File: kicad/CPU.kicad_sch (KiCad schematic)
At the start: 32 parts, among them J1 Conn_01x01_Pin, J2 Conn_01x06_Pin, J3 Conn_01x01_Pin, J4 Conn_01x01_Pin, J5 Conn_01x01_Pin, U10 GAL22V10, U11 AS6C4008-55PCN, U12 AS6C4008-55PCN, U12 GAL22V10, U13 74LS245, U14 74LS245, U3 74LS244, U5 SST39SF040, U6 SST39SF040, U7 68010P10, U8 74LS244, U9 74LS244

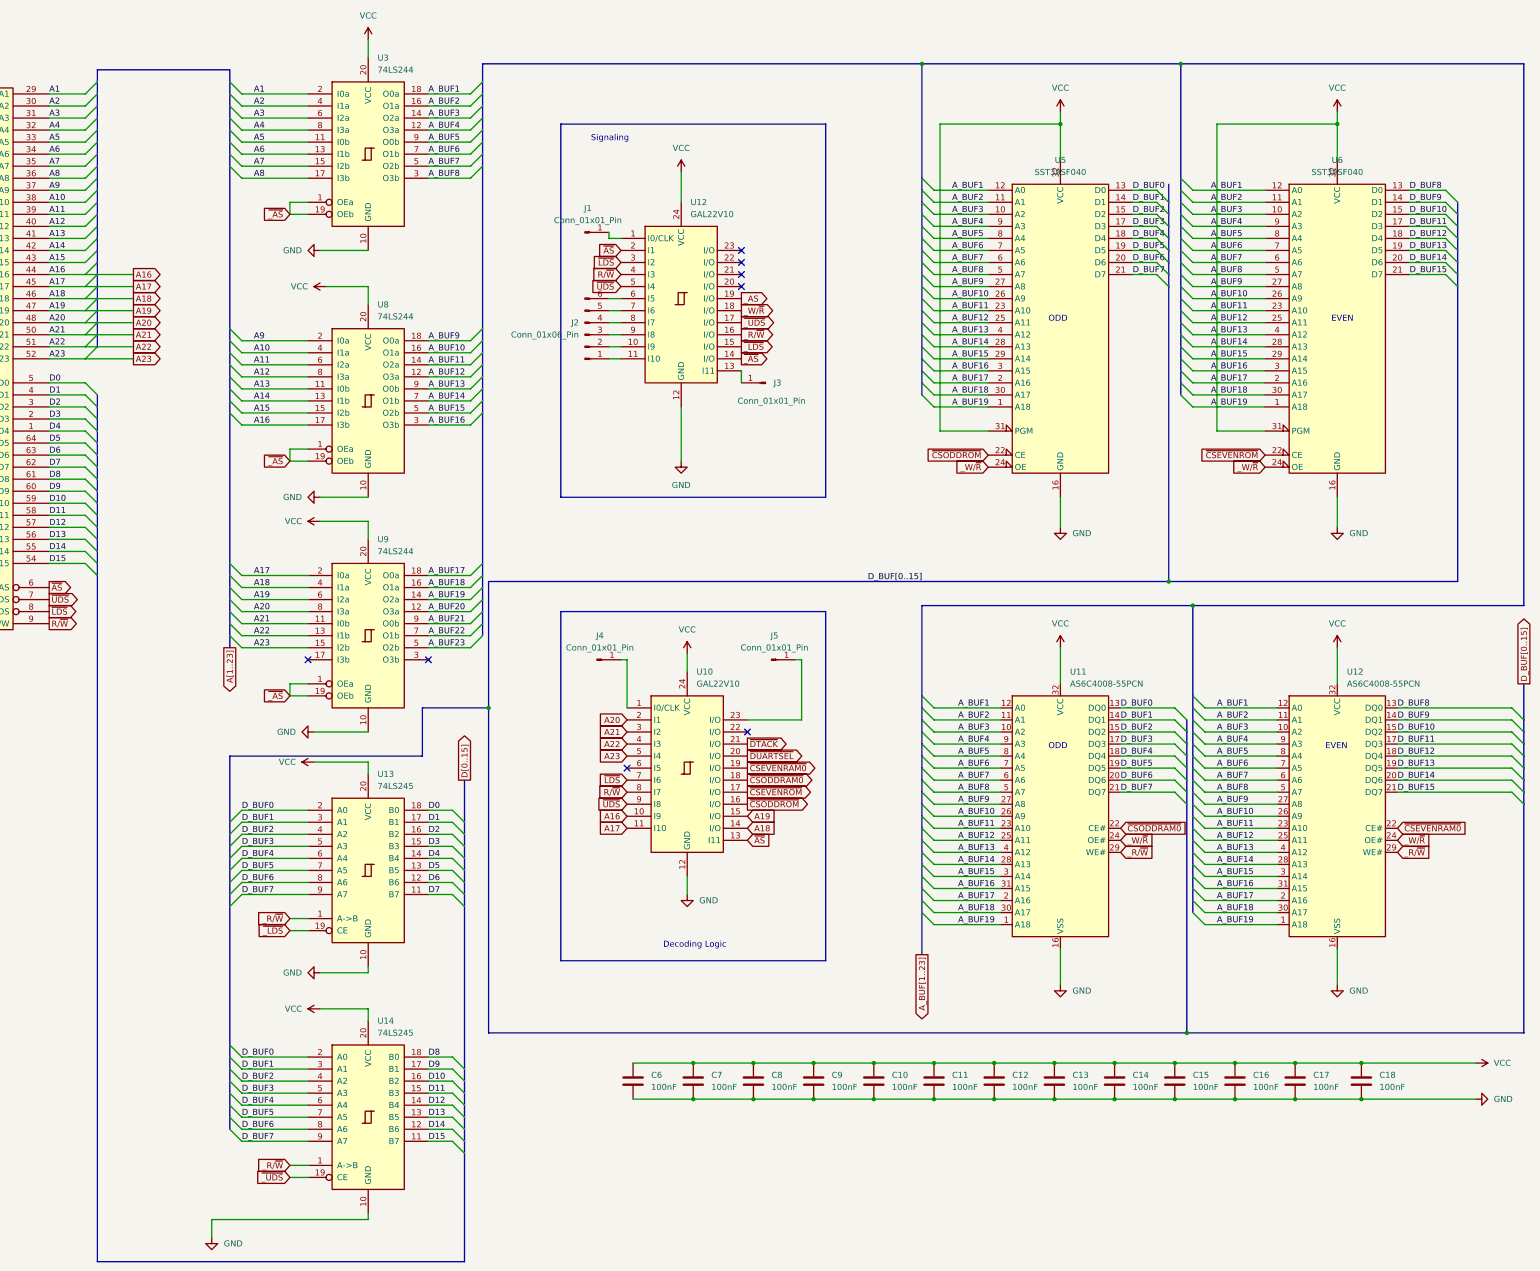
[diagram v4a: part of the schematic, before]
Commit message: PCB to ATX size
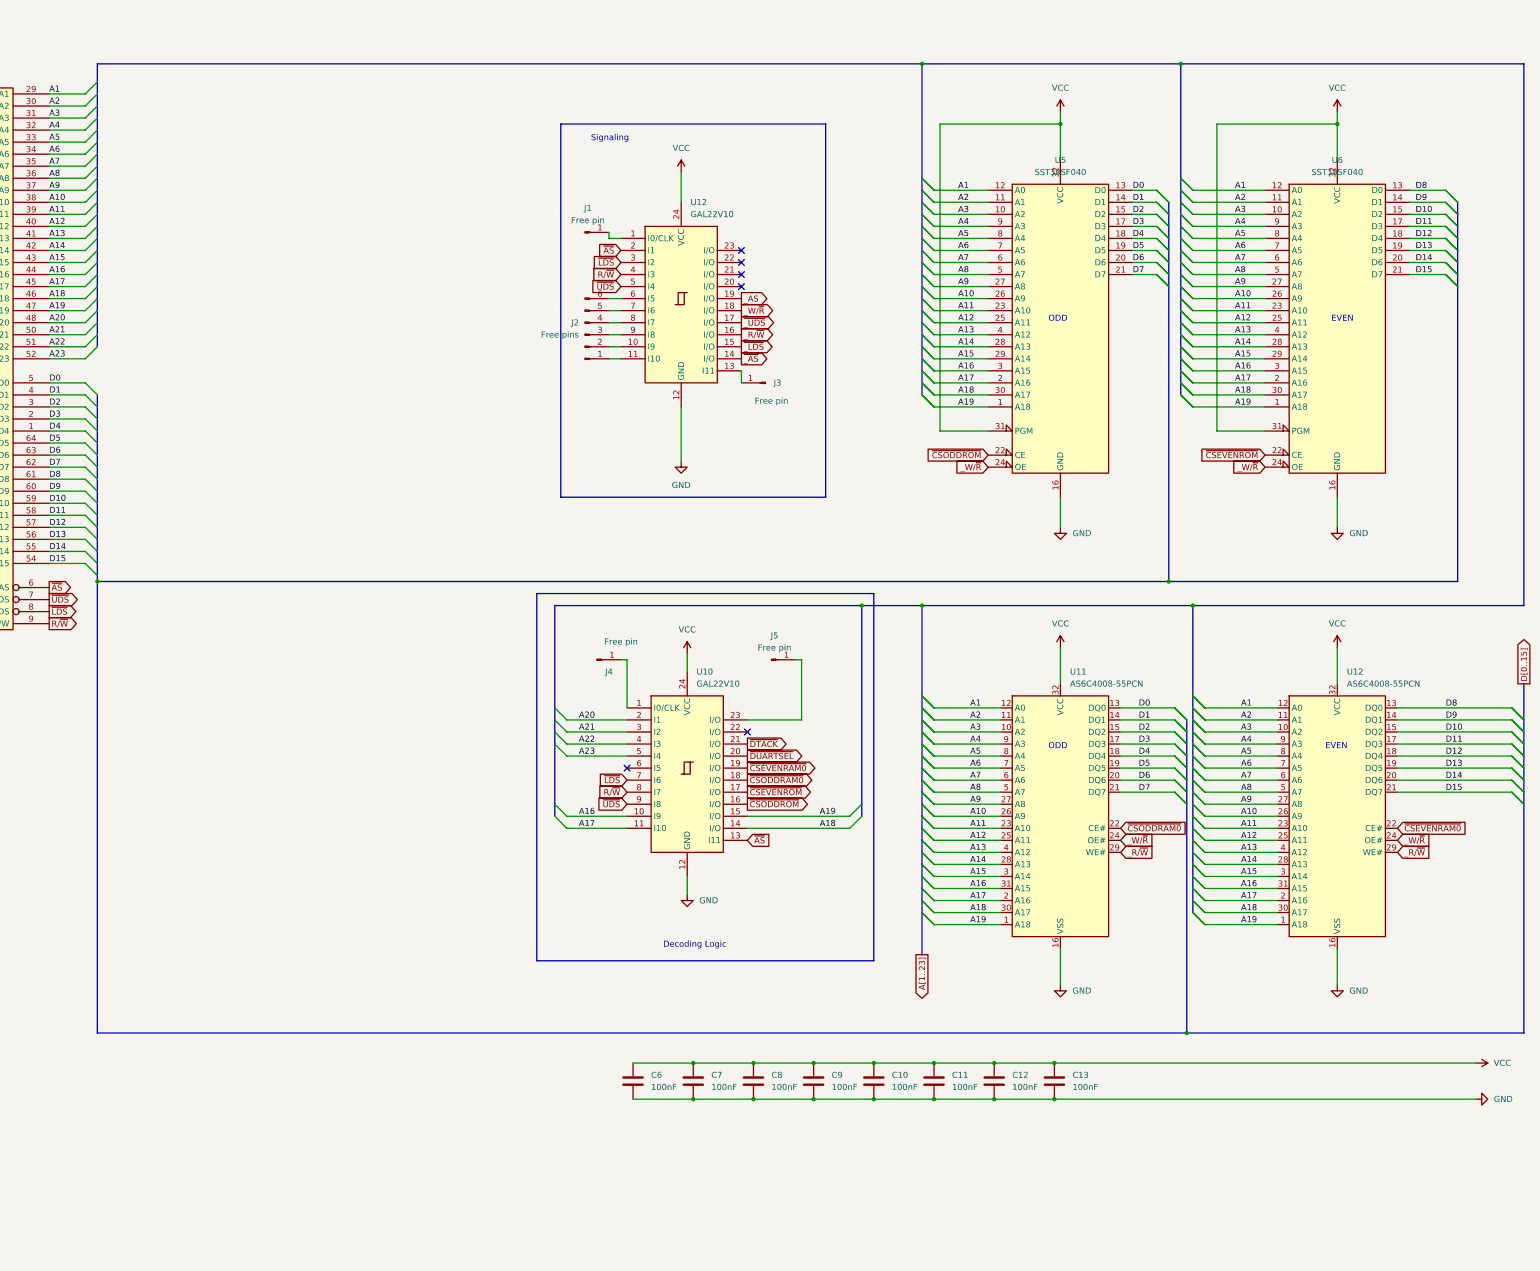
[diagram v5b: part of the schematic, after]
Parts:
- removed C14, C15, C16, C17, C18: 100nF, Capacitor_THT:CP_Radial_D5.0mm_P2.50mm, symbol Device:C
- removed U13, U14: 74LS245, Package_DIP:DIP-20_W7.62mm_Socket, symbol 74xx:74LS245
- removed U3, U8, U9: 74LS244, Package_DIP:DIP-20_W7.62mm_Socket, symbol 74xx:74LS244
- J1, J3, J4, J5: value Conn_01x01_Pin -> Free pin
- J2: value Conn_01x06_Pin -> Free pins
- U7: footprint Package_DIP:DIL64 -> Package_DIP:DIP-64_W25.4mm_Socket
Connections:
- net A_BUF1 is gone; now on net A1: U11.12 (A0), U12.12 (A0), U5.12 (A0), U6.12 (A0)
- net A_BUF10 is gone; now on net A10: U11.26 (A9), U12.26 (A9), U5.26 (A9), U6.26 (A9)
- net A_BUF11 is gone; now on net A11: U11.23 (A10), U12.23 (A10), U5.23 (A10), U6.23 (A10)
- net A_BUF12 is gone; now on net A12: U11.25 (A11), U12.25 (A11), U5.25 (A11), U6.25 (A11)
- net A_BUF13 is gone; now on net A13: U11.4 (A12), U12.4 (A12), U5.4 (A12), U6.4 (A12)
- net A_BUF14 is gone; now on net A14: U11.28 (A13), U12.28 (A13), U5.28 (A13), U6.28 (A13)
- net A_BUF15 is gone; now on net A15: U11.3 (A14), U12.3 (A14), U5.29 (A14), U6.29 (A14)
- net A_BUF16 is gone; now on net A16: U11.31 (A15), U12.31 (A15), U5.3 (A15), U6.3 (A15)
- net A_BUF17 is gone; now on net A17: U11.2 (A16), U12.2 (A16), U5.2 (A16), U6.2 (A16)
- net A_BUF18 is gone; now on net A18: U11.30 (A17), U12.30 (A17), U5.30 (A17), U6.30 (A17)
- net A_BUF19 is gone; now on net A19: U11.1 (A18), U12.1 (A18), U5.1 (A18), U6.1 (A18)
- net A_BUF2 is gone; now on net A2: U11.11 (A1), U12.11 (A1), U5.11 (A1), U6.11 (A1)
- net A_BUF3 is gone; now on net A3: U11.10 (A2), U12.10 (A2), U5.10 (A2), U6.10 (A2)
- net A_BUF4 is gone; now on net A4: U11.9 (A3), U12.9 (A3), U5.9 (A3), U6.9 (A3)
- net A_BUF5 is gone; now on net A5: U11.8 (A4), U12.8 (A4), U5.8 (A4), U6.8 (A4)
- net A_BUF6 is gone; now on net A6: U11.7 (A5), U12.7 (A5), U5.7 (A5), U6.7 (A5)
- net A_BUF7 is gone; now on net A7: U11.6 (A6), U12.6 (A6), U5.6 (A6), U6.6 (A6)
- net A_BUF8 is gone; now on net A8: U11.5 (A7), U12.5 (A7), U5.5 (A7), U6.5 (A7)
- net A_BUF9 is gone; now on net A9: U11.27 (A8), U12.27 (A8), U5.27 (A8), U6.27 (A8)
- net D_BUF0 is gone; now on net D0: U11.13 (DQ0), U5.13 (D0)
- net D_BUF1 is gone; now on net D1: U11.14 (DQ1), U5.14 (D1)
- net D_BUF10 is gone; now on net D10: U12.15 (DQ2), U6.15 (D2)
- net D_BUF11 is gone; now on net D11: U12.17 (DQ3), U6.17 (D3)
- net D_BUF12 is gone; now on net D12: U12.18 (DQ4), U6.18 (D4)
- net D_BUF13 is gone; now on net D13: U12.19 (DQ5), U6.19 (D5)
- net D_BUF14 is gone; now on net D14: U12.20 (DQ6), U6.20 (D6)
- net D_BUF15 is gone; now on net D15: U12.21 (DQ7), U6.21 (D7)
- net D_BUF2 is gone; now on net D2: U11.15 (DQ2), U5.15 (D2)
- net D_BUF3 is gone; now on net D3: U11.17 (DQ3), U5.17 (D3)
- net D_BUF4 is gone; now on net D4: U11.18 (DQ4), U5.18 (D4)
- net D_BUF5 is gone; now on net D5: U11.19 (DQ5), U5.19 (D5)
- net D_BUF6 is gone; now on net D6: U11.20 (DQ6), U5.20 (D6)
- net D_BUF7 is gone; now on net D7: U11.21 (DQ7), U5.21 (D7)
- net D_BUF8 is gone; now on net D8: U12.13 (DQ0), U6.13 (D0)
- net D_BUF9 is gone; now on net D9: U12.14 (DQ1), U6.14 (D1)
- no-connect marks 10 -> 8

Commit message: saving state
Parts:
- C10, C11, C12, C13, C8, C9: footprint Capacitor_THT:CP_Radial_D5.0mm_P2.50mm -> Capacitor_THT:C_Disc_D5.0mm_W2.5mm_P2.50mm
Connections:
- net ~{EXTSEL}: now reaches U10.22 (I/O)
- no-connect marks 8 -> 7

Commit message: fiddlign with placement
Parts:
- C6, C7: footprint Capacitor_THT:CP_Radial_D5.0mm_P2.50mm -> Capacitor_THT:C_Disc_D5.0mm_W2.5mm_P2.50mm
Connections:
- net A16: now also U10.2 (I1); no longer U10.10 (I9)
- net A17: now also U10.3 (I2); no longer U10.11 (I10)
- net A18: now also U10.4 (I3); no longer U10.14 (I/O)
- net A19: now also U10.5 (I4); no longer U10.15 (I/O)
- net A20: now also U10.6 (I5); no longer U10.2 (I1)
- net A21: now also U10.7 (I6); no longer U10.3 (I2)
- net A22: now also U10.8 (I7); no longer U10.4 (I3)
- net A23: now also U10.9 (I8); no longer U10.5 (I4)
- net R/~{W}: now also U10.14 (I/O), U12.2 (I1); no longer U10.8 (I7), U12.4 (I3)
- net ~{AS}: now also U10.10 (I9), U12.5 (I4); no longer U10.13 (I11), U12.2 (I1)
- net ~{LDS}: now also U10.15 (I/O); no longer U10.7 (I6)
- net ~{UDS}: now also U10.11 (I10), U12.4 (I3); no longer U10.9 (I8), U12.5 (I4)

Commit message: got irq to work
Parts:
- removed J5: Free pin, Connector_PinSocket_2.54mm:PinSocket_1x01_P2.54mm_Vertical, symbol Connector:Conn_01x01_Pin
- added J5: Free pins, Connector_PinSocket_2.54mm:PinSocket_1x05_P2.54mm_Vertical, symbol Connector:Conn_01x05_Pin
- U5, U6: footprint Package_DIP:DIP-32_W15.24mm_Socket -> Socket:DIP_Socket-32_W11.9_W12.7_W15.24_W17.78_W18.5_3M_232-1285-00-0602J
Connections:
- net _AS: now also U12.18 (I/O); no longer U12.19 (I/O)
- net _W/~{R}: now also U10.23 (I/O); no longer U12.18 (I/O)
- net at U12.20 (I/O): now also J5.2 (Pin_2)
- net at U12.21 (I/O): now also J5.3 (Pin_3)
- net at U12.22 (I/O): now also J5.4 (Pin_4)
- net at U12.23 (I/O): now also J5.5 (Pin_5)
- new net: J5.1 (Pin_1), U12.19 (I/O)
- no-connect marks 7 -> 3
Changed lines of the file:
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@@
   (junction (at 331.47 229.87) (diameter 0) (color 0 0 0 0)
   )
-  (no_connect (at 237.49 64.77))
-  (no_connect (at 237.49 67.31))
   (no_connect (at 40.64 74.93))
   (no_connect (at 238.76 189.23))
-  (no_connect (at 237.49 72.39))
-  (no_connect (at 237.49 69.85))
   (no_connect (at 40.64 52.07))
   (bus_entry (at 275.59 57.15) (size 2.54 2.54)
@@
     (stroke (width 0) (type default))
   )
-  (wire (pts (xy 250.19 151.13) (xy 250.19 163.83))
-    (stroke (width 0) (type default))
-  )
   (bus (pts (xy 101.6 102.87) (xy 101.6 105.41))
     (stroke (width 0) (type default))
@@
     (stroke (width 0) (type default))
   )
-  (wire (pts (xy 238.76 163.83) (xy 250.19 163.83))
-    (stroke (width 0) (type default))
-  )
   (wire (pts (xy 39.37 102.87) (xy 40.64 102.87))
     (stroke (width 0) (type default))
@@
     (stroke (width 0) (type default))
   )
-  (wire (pts (xy 248.92 151.13) (xy 250.19 151.13))
-    (stroke (width 0) (type default))
-  )
   (bus (pts (xy 275.59 87.63) (xy 275.59 90.17))
     (stroke (width 0) (type default))
@@
     (effects (font (size 1.27 1.27)) (justify left bottom))
   )
-  (label "A16" (at 205.74 163.83 0)
+  (label "A16" (at 205.74 163.83 0) (fields_autoplaced)
     (effects (font (size 1.27 1.27)) (justify left bottom))
   )
@@
     (effects (font (size 1.27 1.27)) (justify left bottom))
   )
-  (label "A20" (at 205.74 173.99 0)
+  (label "A20" (at 205.74 173.99 0) (fields_autoplaced)
     (effects (font (size 1.27 1.27)) (justify left bottom))
   )
@@
     (effects (font (size 1.27 1.27)) (justify left bottom))
   )
-  (label "A18" (at 205.74 168.91 0)
+  (label "A18" (at 205.74 168.91 0) (fields_autoplaced)
     (effects (font (size 1.27 1.27)) (justify left bottom))
   )
@@
     (effects (font (size 1.27 1.27)) (justify left bottom))
   )
-  (label "A22" (at 205.74 179.07 0)
+  (label "A22" (at 205.74 179.07 0) (fields_autoplaced)
     (effects (font (size 1.27 1.27)) (justify left bottom))
   )
@@
     (effects (font (size 1.27 1.27)) (justify left bottom))
   )
-  (label "A21" (at 205.74 176.53 0)
+  (label "A21" (at 205.74 176.53 0) (fields_autoplaced)
     (effects (font (size 1.27 1.27)) (justify left bottom))
   )
@@
     (effects (font (size 1.27 1.27)) (justify left bottom))
   )
-  (label "A19" (at 205.74 171.45 0)
+  (label "A19" (at 205.74 171.45 0) (fields_autoplaced)
     (effects (font (size 1.27 1.27)) (justify left bottom))
   )
@@
     (effects (font (size 1.27 1.27)) (justify left bottom))
   )
-  (label "A23" (at 205.74 181.61 0)
+  (label "A23" (at 205.74 181.61 0) (fields_autoplaced)
     (effects (font (size 1.27 1.27)) (justify left bottom))
   )
@@
     (effects (font (size 1.27 1.27)) (justify left bottom))
   )
-  (label "A17" (at 205.74 166.37 0)
+  (label "A17" (at 205.74 166.37 0) (fields_autoplaced)
     (effects (font (size 1.27 1.27)) (justify left bottom))
   )
@@
     )
   )
-  (global_label "_W{slash}~{R}" (shape output) (at 237.49 77.47 0) (fields_autoplaced)
+  (global_label "_W{slash}~{R}" (shape output) (at 238.76 163.83 0) (fields_autoplaced)
     (effects (font (size 1.27 1.27)) (justify left))
-    (property "Intersheetrefs" "${INTERSHEET_REFS}" (at 245.4153 77.47 0)
+    (property "Intersheetrefs" "${INTERSHEET_REFS}" (at 246.6853 163.83 0)
       (effects (font (size 1.27 1.27)) (justify left) hide)
     )
@@
     )
   )
-  (global_label "_AS" (shape output) (at 237.49 74.93 0) (fields_autoplaced)
+  (global_label "_AS" (shape output) (at 237.49 77.47 0) (fields_autoplaced)
     (effects (font (size 1.27 1.27)) (justify left))
-    (property "Intersheetrefs" "${INTERSHEET_REFS}" (at 243.6615 74.93 0)
+    (property "Intersheetrefs" "${INTERSHEET_REFS}" (at 243.6615 77.47 0)
       (effects (font (size 1.27 1.27)) (justify left) hide)
     )
@@
       (effects (font (size 1.27 1.27)))
     )
-    (property "Footprint" "Package_DIP:DIP-32_W15.24mm_Socket" (at 304.8 74.93 0)
+    (property "Footprint" "Socket:DIP_Socket-32_W11.9_W12.7_W15.24_W17.78_W18.5_3M_232-1285-00-0602J" (at 304.8 74.93 0)
       (effects (font (size 1.27 1.27)) hide)
     )
@@
       (effects (font (size 1.27 1.27)))
     )
-    (property "Footprint" "Package_DIP:DIP-32_W15.24mm_Socket" (at 363.22 74.93 0)
+    (property "Footprint" "Socket:DIP_Socket-32_W11.9_W12.7_W15.24_W17.78_W18.5_3M_232-1285-00-0602J" (at 363.22 74.93 0)
       (effects (font (size 1.27 1.27)) hide)
     )
@@
     )
   )
-  (symbol (lib_id "power:VCC") (at 304.8 148.59 0) (unit 1)
+  (symbol (lib_id "Connector:Conn_01x05_Pin") (at 242.57 69.85 180) (unit 1)
     (in_bom yes) (on_board yes) (dnp no) (fields_autoplaced)
-    (property "Reference" "#PWR024" (at 304.8 152.4 0)
-      (effects (font (size 1.27 1.27)) hide)
+    (property "Reference" "J5" (at 243.84 68.58 0)
+      (effects (font (size 1.27 1.27)) (justify right))
     )
-    (property "Value" "VCC" (at 304.8 143.51 0)
-      (effects (font (size 1.27 1.27)))
+    (property "Value" "Free pins" (at 243.84 71.12 0)
+      (effects (font (size 1.27 1.27)) (justify right))
     )
-    (property "Footprint" "" (at 304.8 148.59 0)
+    (property "Footprint" "Connector_PinSocket_2.54mm:PinSocket_1x05_P2.54mm_Vertical" (at 242.57 69.85 0)
       (effects (font (size 1.27 1.27)) hide)
     )
-    (property "Datasheet" "" (at 304.8 148.59 0)
+    (property "Datasheet" "~" (at 242.57 69.85 0)
       (effects (font (size 1.27 1.27)) hide)
     )
     (pin "1")
+    (pin "2")
+    (pin "3")
+    (pin "4")
+    (pin "5")
     (instances
       (project "mb68k"
         (path "/e63e39d7-6ac0-4ffd-8aa3-1841a4541b55/c0b233c3-0354-40a8-9da4-8134543aeba9"
-          (reference "#PWR024") (unit 1)
+          (reference "J5") (unit 1)
         )
       )
     )
   )
-  (symbol (lib_id "power:VCC") (at 363.22 148.59 0) (unit 1)
+  (symbol (lib_id "power:VCC") (at 304.8 148.59 0) (unit 1)
     (in_bom yes) (on_board yes) (dnp no) (fields_autoplaced)
-    (property "Reference" "#PWR025" (at 363.22 152.4 0)
+    (property "Reference" "#PWR024" (at 304.8 152.4 0)
       (effects (font (size 1.27 1.27)) hide)
     )
-    (property "Value" "VCC" (at 363.22 143.51 0)
+    (property "Value" "VCC" (at 304.8 143.51 0)
       (effects (font (size 1.27 1.27)))
     )
-    (property "Footprint" "" (at 363.22 148.59 0)
+    (property "Footprint" "" (at 304.8 148.59 0)
       (effects (font (size 1.27 1.27)) hide)
     )
-    (property "Datasheet" "" (at 363.22 148.59 0)
+    (property "Datasheet" "" (at 304.8 148.59 0)
       (effects (font (size 1.27 1.27)) hide)
     )
@@
       (project "mb68k"
         (path "/e63e39d7-6ac0-4ffd-8aa3-1841a4541b55/c0b233c3-0354-40a8-9da4-8134543aeba9"
-          (reference "#PWR025") (unit 1)
+          (reference "#PWR024") (unit 1)
         )
       )
     )
   )
-  (symbol (lib_id "Connector:Conn_01x01_Pin") (at 243.84 151.13 0) (unit 1)
+  (symbol (lib_id "power:VCC") (at 363.22 148.59 0) (unit 1)
     (in_bom yes) (on_board yes) (dnp no) (fields_autoplaced)
-    (property "Reference" "J5" (at 244.475 146.05 0)
-      (effects (font (size 1.27 1.27)))
+    (property "Reference" "#PWR025" (at 363.22 152.4 0)
+      (effects (font (size 1.27 1.27)) hide)
     )
-    (property "Value" "Free pin" (at 244.475 148.59 0)
+    (property "Value" "VCC" (at 363.22 143.51 0)
       (effects (font (size 1.27 1.27)))
     )
-    (property "Footprint" "Connector_PinSocket_2.54mm:PinSocket_1x01_P2.54mm_Vertical" (at 243.84 151.13 0)
+    (property "Footprint" "" (at 363.22 148.59 0)
       (effects (font (size 1.27 1.27)) hide)
     )
-    (property "Datasheet" "~" (at 243.84 151.13 0)
+    (property "Datasheet" "" (at 363.22 148.59 0)
       (effects (font (size 1.27 1.27)) hide)
     )
@@
       (project "mb68k"
         (path "/e63e39d7-6ac0-4ffd-8aa3-1841a4541b55/c0b233c3-0354-40a8-9da4-8134543aeba9"
-          (reference "J5") (unit 1)
+          (reference "#PWR025") (unit 1)
         )
       )
